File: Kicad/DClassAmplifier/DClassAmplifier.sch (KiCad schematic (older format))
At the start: 21 parts, among them J1 Conn_01x02, J2 Conn_01x03, J3 Conn_01x02, J4 Conn_01x02, J5 Conn_01x02

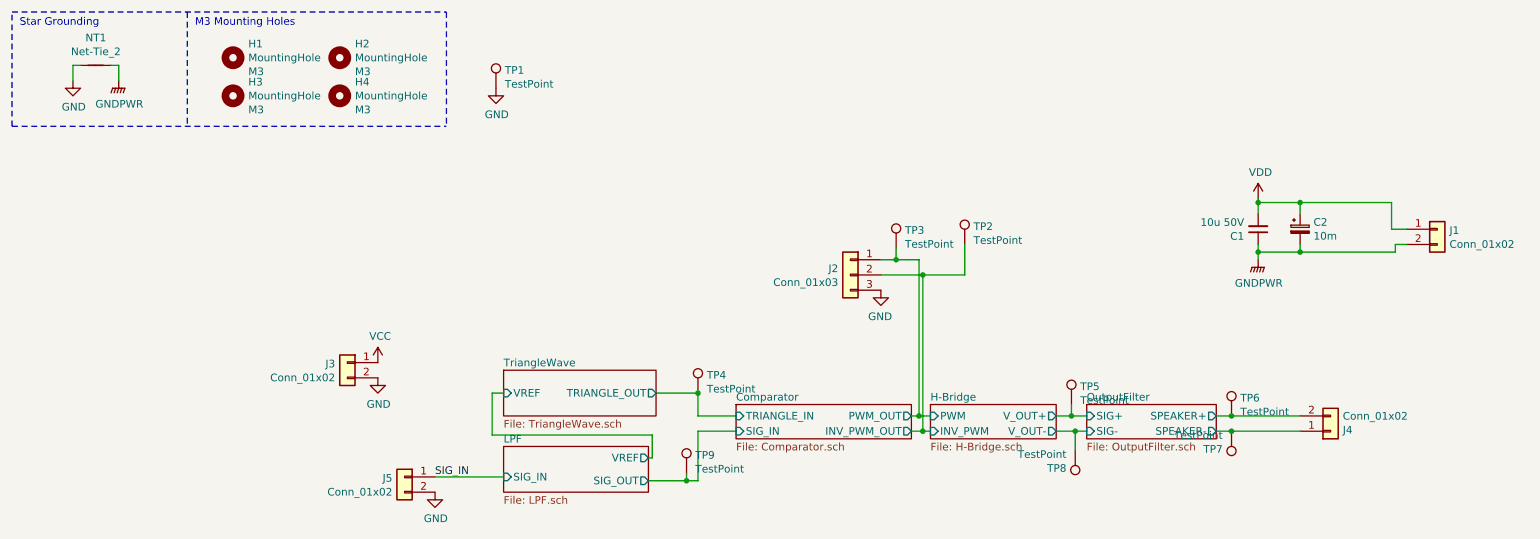
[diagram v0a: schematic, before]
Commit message: Add 10V Reg and Reroute
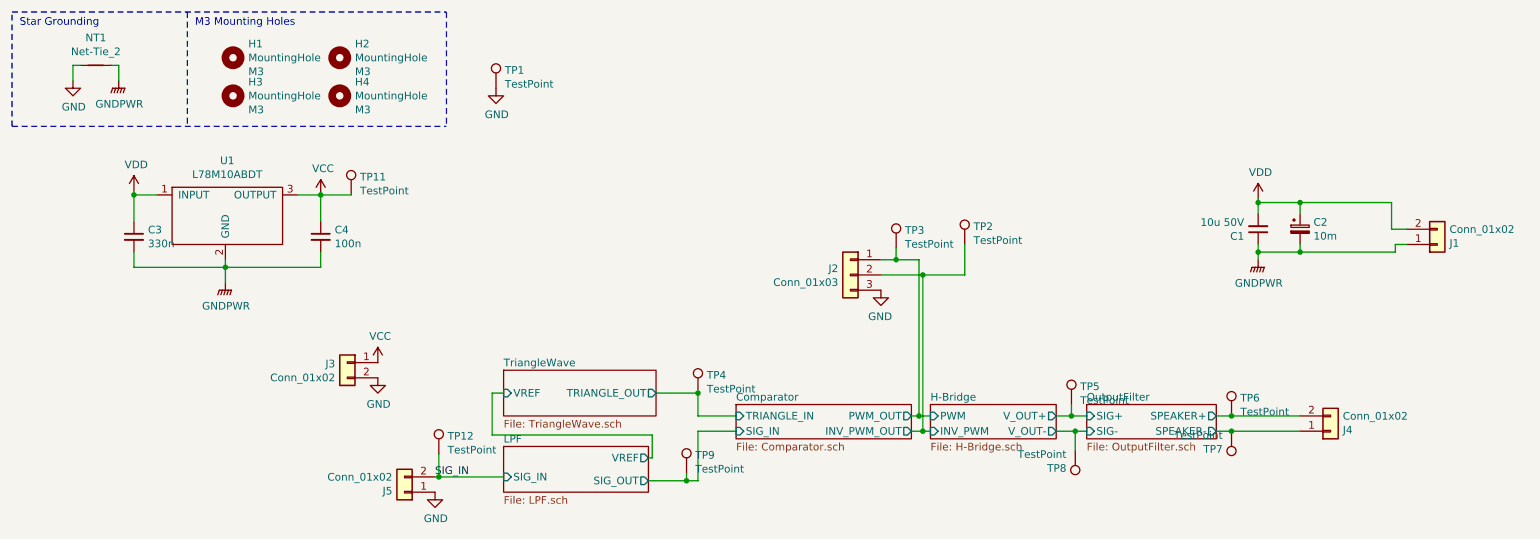
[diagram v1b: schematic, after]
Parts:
- added C3: 330n, Capacitor_SMD:C_0603_1608Metric_Pad1.08x0.95mm_HandSolder, symbol Device:C_Small
- added C4: 100n, Capacitor_SMD:C_0603_1608Metric_Pad1.08x0.95mm_HandSolder, symbol Device:C_Small
- added TP11, TP12: TestPoint, TestPoint:TestPoint_THTPad_D1.5mm_Drill0.7mm, symbol Connector:TestPoint
- added U1: L78M10ABDT, Package_TO_SOT_SMD:TO-252-2, symbol L78M10ABDT:L78M10ABDT
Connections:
- net GND: now also J5.1 (Pin_1); no longer J5.2 (Pin_2)
- net GNDPWR: now also J1.1 (Pin_1), C3.2, C4.2, U1.2 (GND); no longer J1.2 (Pin_2)
- net SIG_IN: now also J5.2 (Pin_2), TP12.1; no longer J5.1 (Pin_1)
- net VCC: now also C4.1, TP11.1, U1.3 (OUTPUT)
- net VDD: now also J1.2 (Pin_2), C3.1, U1.1 (INPUT); no longer J1.1 (Pin_1)

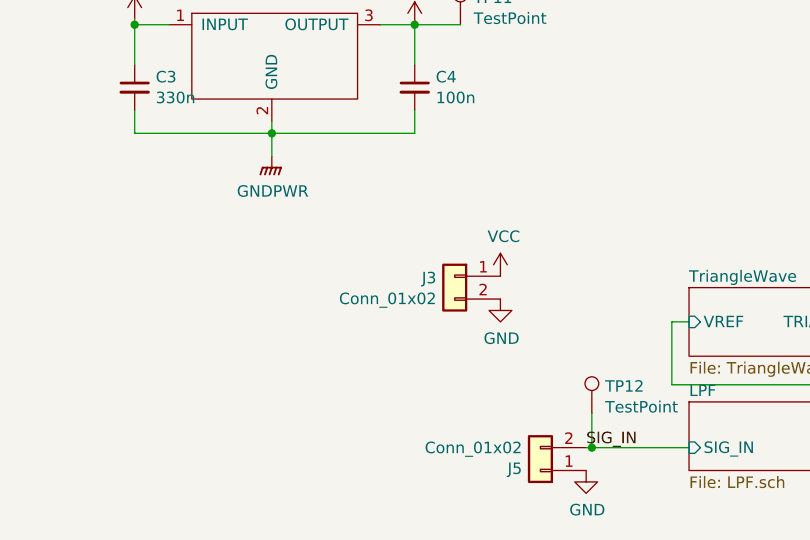
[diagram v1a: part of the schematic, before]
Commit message: Graphics and SilkScreen Improvement
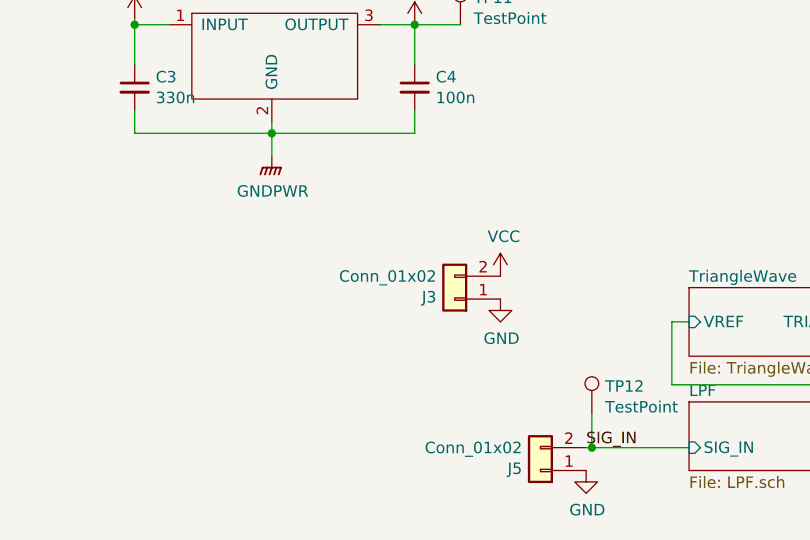
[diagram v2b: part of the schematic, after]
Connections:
- net GND: now also J3.1 (Pin_1); no longer J3.2 (Pin_2)
- net VCC: now also J3.2 (Pin_2); no longer J3.1 (Pin_1)
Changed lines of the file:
@@
 L Connector_Generic:Conn_01x02 J?
 U 1 1 611C90F1
-P 2850 2900
+P 2850 3000
 AR Path="/611D4178/611C90F1" Ref="J?"  Part="1"
 AR Path="/610C616D/611C90F1" Ref="J?"  Part="1"
 AR Path="/611C90F1" Ref="J3"  Part="1"
-F 0 "J3" H 2930 2892 50  0000 L CNN
-F 1 "Conn_01x02" H 2930 2801 50  0000 L CNN
-F 2 "TerminalBlock:TerminalBlock_bornier-2_P5.08mm" H 2850 2900 50  0001 C CNN
-F 3 "~" H 2850 2900 50  0001 C CNN
-	1    2850 2900
-	-1   0    0    -1
+F 0 "J3" H 2930 2992 50  0000 L CNN
+F 1 "Conn_01x02" H 2930 2901 50  0000 L CNN
+F 2 "TerminalBlock:TerminalBlock_bornier-2_P5.08mm" H 2850 3000 50  0001 C CNN
+F 3 "~" H 2850 3000 50  0001 C CNN
+	1    2850 3000
+	-1   0    0    1
 $EndComp
 $Comp
